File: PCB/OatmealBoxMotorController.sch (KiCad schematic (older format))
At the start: 2 parts

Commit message: Added second motor driver. Got everything hooked up back.
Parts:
- added U7: TB6612FNG, symbol TB6612FNG
- gave numbers to parts that had none: 2
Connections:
- net +12V: now also U7.13 (VM2), U7.14 (VM3), U7.24 (VM1)
- net +3V3: now also U7.19 (STBY), U7.20 (VCC)
- net GND: now also U7.10 (PGND2), U7.18 (GND), U7.3 (PGND1), U7.4 (PGND1), U7.9 (PGND2)
- net at U5.15 (PWM8): now also U7.23 (PWMA)
- net at U5.16 (PWM9): now also U7.22 (AIN2)
- net at U5.17 (PWM10): now also U7.21 (AIN1)
- net at U5.18 (PWM11): now also U7.17 (BIN1)
- net at U5.19 (PWM12): now also U7.16 (BIN2)
- net at U5.20 (PWM13): now also U7.15 (PWMB)
- net ePWM3: now reaches U5.21 (PWM14)
- net ePWM4: now reaches U5.22 (PWM15)
- net ePWM1: now reaches U5.6 (PWM0)
- net ePWM2: now reaches U5.7 (PWM1)
- new net Motor3+: U7.1 (AO1), U7.2 (AO1)
- new net Motor3-: U7.5 (AO2), U7.6 (AO2)
- new net Motor4+: U7.7 (BO2), U7.8 (BO2)
- new net Motor4-: U7.11 (BO1), U7.12 (BO1)
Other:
- moved on the sheet: U5

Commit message: Connected I2C, fixed ERC errors
Connected I2C to the PWM controller.
Fixed ERC errors.
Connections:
- net SCL: now reaches U5.26 (SCL)
- net SDA: now reaches U5.27 (SDA)
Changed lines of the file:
@@
 $EndComp
 $Comp
-L +3.3V #PWR026
+L +3.3V #PWR029
 U 1 1 5B4A7AD7
 P 1000 1450
-F 0 "#PWR026" H 1000 1300 50  0001 C CNN
+F 0 "#PWR029" H 1000 1300 50  0001 C CNN
 F 1 "+3.3V" H 1000 1590 50  0000 C CNN
 F 2 "" H 1000 1450 50  0001 C CNN
@@
 $EndComp
 $Comp
-L GND #PWR027
+L GND #PWR030
 U 1 1 5B4A7AED
 P 950 2250
-F 0 "#PWR027" H 950 2000 50  0001 C CNN
+F 0 "#PWR030" H 950 2000 50  0001 C CNN
 F 1 "GND" H 950 2100 50  0000 C CNN
 F 2 "" H 950 2250 50  0001 C CNN
@@
 $EndComp
 $Comp
-L GND #PWR028
+L GND #PWR031
 U 1 1 5B4A7B03
 P 950 3200
-F 0 "#PWR028" H 950 2950 50  0001 C CNN
+F 0 "#PWR031" H 950 2950 50  0001 C CNN
 F 1 "GND" H 950 3050 50  0000 C CNN
 F 2 "" H 950 3200 50  0001 C CNN
@@
 Connection ~ 1100 2800
 $Comp
-L +3.3V #PWR029
+L +3.3V #PWR032
 U 1 1 5B4A7BB0
 P 950 3000
-F 0 "#PWR029" H 950 2850 50  0001 C CNN
+F 0 "#PWR032" H 950 2850 50  0001 C CNN
 F 1 "+3.3V" H 950 3140 50  0000 C CNN
 F 2 "" H 950 3000 50  0001 C CNN
@@
 $EndComp
 $Comp
-L +12V #PWR030
+L +12V #PWR033
 U 1 1 5B4D75A1
 P 4700 1500
-F 0 "#PWR030" H 4700 1350 50  0001 C CNN
+F 0 "#PWR033" H 4700 1350 50  0001 C CNN
 F 1 "+12V" H 4700 1640 50  0000 C CNN
 F 2 "" H 4700 1500 50  0001 C CNN
@@
 $EndComp
 $Comp
-L +12V #PWR031
+L +12V #PWR034
 U 1 1 5B4D75BD
 P 4700 3300
-F 0 "#PWR031" H 4700 3150 50  0001 C CNN
+F 0 "#PWR034" H 4700 3150 50  0001 C CNN
 F 1 "+12V" H 4700 3440 50  0000 C CNN
 F 2 "" H 4700 3300 50  0001 C CNN
@@
 Connection ~ 4800 3300
 $Comp
-L +3.3V #PWR032
+L +3.3V #PWR035
 U 1 1 5B4D7628
 P 4700 2400
-F 0 "#PWR032" H 4700 2250 50  0001 C CNN
+F 0 "#PWR035" H 4700 2250 50  0001 C CNN
 F 1 "+3.3V" H 4700 2540 50  0000 C CNN
 F 2 "" H 4700 2400 50  0001 C CNN
@@
 Connection ~ 4750 2400
 $Comp
-L GND #PWR033
+L GND #PWR036
 U 1 1 5B4D76CA
 P 4650 2600
-F 0 "#PWR033" H 4650 2350 50  0001 C CNN
+F 0 "#PWR036" H 4650 2350 50  0001 C CNN
 F 1 "GND" H 4650 2450 50  0000 C CNN
 F 2 "" H 4650 2600 50  0001 C CNN
@@
 $EndComp
 $Comp
-L GND #PWR034
+L GND #PWR037
 U 1 1 5B4D76E6
 P 6200 2900
-F 0 "#PWR034" H 6200 2650 50  0001 C CNN
+F 0 "#PWR037" H 6200 2650 50  0001 C CNN
 F 1 "GND" H 6200 2750 50  0000 C CNN
 F 2 "" H 6200 2900 50  0001 C CNN
@@
 $EndComp
 $Comp
-L GND #PWR035
+L GND #PWR038
 U 1 1 5B4D7702
 P 6200 2000
-F 0 "#PWR035" H 6200 1750 50  0001 C CNN
+F 0 "#PWR038" H 6200 1750 50  0001 C CNN
 F 1 "GND" H 6200 1850 50  0000 C CNN
 F 2 "" H 6200 2000 50  0001 C CNN
@@
 $EndComp
 $Comp
-L +12V #PWR036
+L +12V #PWR039
 U 1 1 5B4EDBEA
 P 4750 3700
-F 0 "#PWR036" H 4750 3550 50  0001 C CNN
+F 0 "#PWR039" H 4750 3550 50  0001 C CNN
 F 1 "+12V" H 4750 3840 50  0000 C CNN
 F 2 "" H 4750 3700 50  0001 C CNN
@@
 $EndComp
 $Comp
-L +12V #PWR037
+L +12V #PWR040
 U 1 1 5B4EDBF0
 P 4750 5500
-F 0 "#PWR037" H 4750 5350 50  0001 C CNN
+F 0 "#PWR040" H 4750 5350 50  0001 C CNN
 F 1 "+12V" H 4750 5640 50  0000 C CNN
 F 2 "" H 4750 5500 50  0001 C CNN
@@
 Connection ~ 4850 5500
 $Comp
-L +3.3V #PWR038
+L +3.3V #PWR041
 U 1 1 5B4EDBFC
 P 4750 4600
-F 0 "#PWR038" H 4750 4450 50  0001 C CNN
+F 0 "#PWR041" H 4750 4450 50  0001 C CNN
 F 1 "+3.3V" H 4750 4740 50  0000 C CNN
 F 2 "" H 4750 4600 50  0001 C CNN
@@
 Connection ~ 4800 4600
 $Comp
-L GND #PWR039
+L GND #PWR042
 U 1 1 5B4EDC06
 P 4700 4800
-F 0 "#PWR039" H 4700 4550 50  0001 C CNN
+F 0 "#PWR042" H 4700 4550 50  0001 C CNN
 F 1 "GND" H 4700 4650 50  0000 C CNN
 F 2 "" H 4700 4800 50  0001 C CNN
@@
 $EndComp
 $Comp
-L GND #PWR040
+L GND #PWR043
 U 1 1 5B4EDC0C
 P 6250 5100
-F 0 "#PWR040" H 6250 4850 50  0001 C CNN
+F 0 "#PWR043" H 6250 4850 50  0001 C CNN
 F 1 "GND" H 6250 4950 50  0000 C CNN
 F 2 "" H 6250 5100 50  0001 C CNN
@@
 $EndComp
 $Comp
-L GND #PWR041
+L GND #PWR044
 U 1 1 5B4EDC12
 P 6250 4200
-F 0 "#PWR041" H 6250 3950 50  0001 C CNN
+F 0 "#PWR044" H 6250 3950 50  0001 C CNN
 F 1 "GND" H 6250 4050 50  0000 C CNN
 F 2 "" H 6250 4200 50  0001 C CNN
@@
 Wire Wire Line
 	2550 3200 2400 3200
+Text HLabel 1100 1900 0    60   BiDi ~ 0
+SDA
+Text HLabel 1100 2050 0    60   Input ~ 0
+SCL
+Wire Wire Line
+	1200 1900 1100 1900
+Wire Wire Line
+	1200 2050 1100 2050
 $EndSCHEMATC

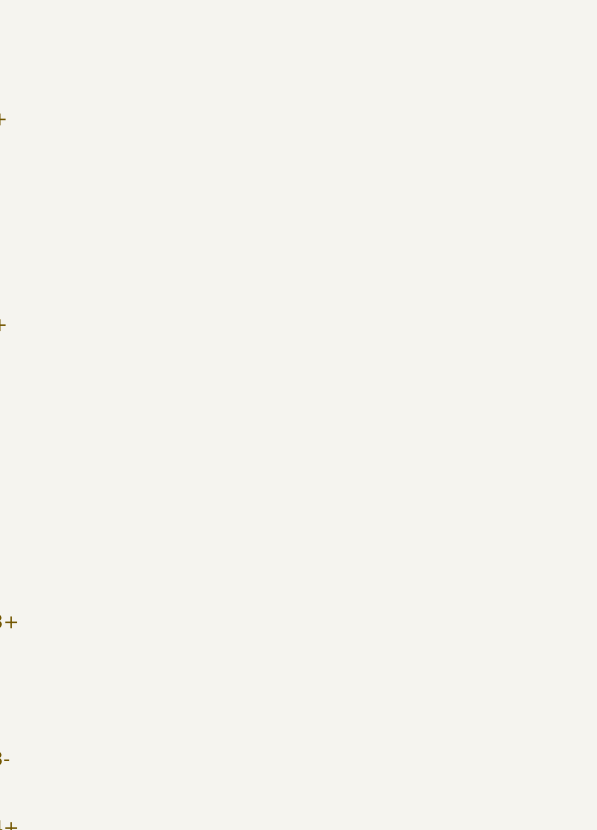
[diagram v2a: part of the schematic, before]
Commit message: Added caps for the motor drivers
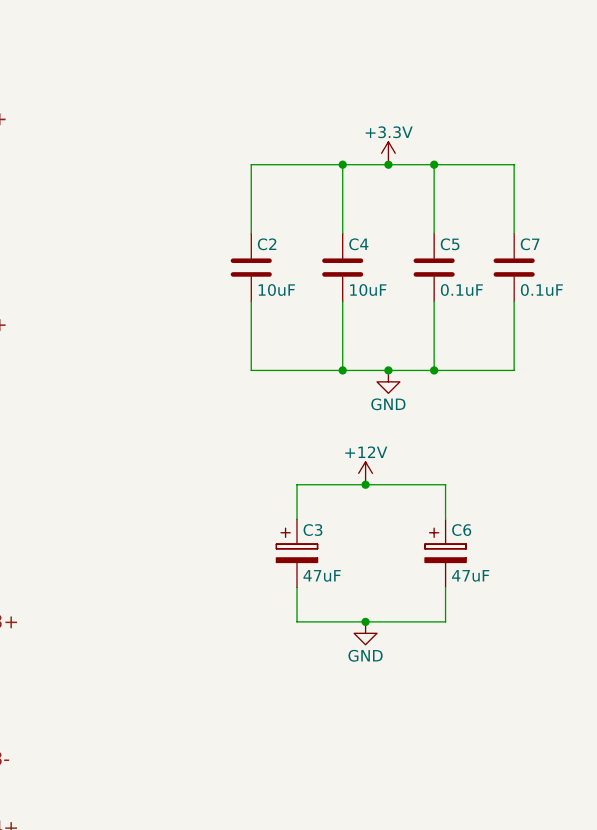
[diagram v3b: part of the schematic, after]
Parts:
- added C2, C4: 10uF, symbol C
- added C3, C6: 47uF, symbol CP
- added C5, C7: 0.1uF, symbol C
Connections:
- net +12V: now also C3.1, C6.1
- net +3V3: now also C2.1, C4.1, C5.1, C7.1
- net GND: now also C2.2, C3.2, C4.2, C5.2, C6.2, C7.2
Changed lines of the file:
@@
 $EndComp
 $Comp
-L +3.3V #PWR029
+L +3.3V #PWR32
 U 1 1 5B4A7AD7
 P 1000 1450
-F 0 "#PWR029" H 1000 1300 50  0001 C CNN
+F 0 "#PWR32" H 1000 1300 50  0001 C CNN
 F 1 "+3.3V" H 1000 1590 50  0000 C CNN
 F 2 "" H 1000 1450 50  0001 C CNN
@@
 $EndComp
 $Comp
-L GND #PWR030
+L GND #PWR29
 U 1 1 5B4A7AED
 P 950 2250
-F 0 "#PWR030" H 950 2000 50  0001 C CNN
+F 0 "#PWR29" H 950 2000 50  0001 C CNN
 F 1 "GND" H 950 2100 50  0000 C CNN
 F 2 "" H 950 2250 50  0001 C CNN
@@
 $EndComp
 $Comp
-L GND #PWR031
+L GND #PWR31
 U 1 1 5B4A7B03
 P 950 3200
-F 0 "#PWR031" H 950 2950 50  0001 C CNN
+F 0 "#PWR31" H 950 2950 50  0001 C CNN
 F 1 "GND" H 950 3050 50  0000 C CNN
 F 2 "" H 950 3200 50  0001 C CNN
@@
 Connection ~ 1100 2800
 $Comp
-L +3.3V #PWR032
+L +3.3V #PWR30
 U 1 1 5B4A7BB0
 P 950 3000
-F 0 "#PWR032" H 950 2850 50  0001 C CNN
+F 0 "#PWR30" H 950 2850 50  0001 C CNN
 F 1 "+3.3V" H 950 3140 50  0000 C CNN
 F 2 "" H 950 3000 50  0001 C CNN
@@
 $EndComp
 $Comp
-L +12V #PWR033
+L +12V #PWR34
 U 1 1 5B4D75A1
 P 4700 1500
-F 0 "#PWR033" H 4700 1350 50  0001 C CNN
+F 0 "#PWR34" H 4700 1350 50  0001 C CNN
 F 1 "+12V" H 4700 1640 50  0000 C CNN
 F 2 "" H 4700 1500 50  0001 C CNN
@@
 $EndComp
 $Comp
-L +12V #PWR034
+L +12V #PWR36
 U 1 1 5B4D75BD
 P 4700 3300
-F 0 "#PWR034" H 4700 3150 50  0001 C CNN
+F 0 "#PWR36" H 4700 3150 50  0001 C CNN
 F 1 "+12V" H 4700 3440 50  0000 C CNN
 F 2 "" H 4700 3300 50  0001 C CNN
@@
 Connection ~ 4800 3300
 $Comp
-L +3.3V #PWR035
+L +3.3V #PWR35
 U 1 1 5B4D7628
 P 4700 2400
-F 0 "#PWR035" H 4700 2250 50  0001 C CNN
+F 0 "#PWR35" H 4700 2250 50  0001 C CNN
 F 1 "+3.3V" H 4700 2540 50  0000 C CNN
 F 2 "" H 4700 2400 50  0001 C CNN
@@
 Connection ~ 4750 2400
 $Comp
-L GND #PWR036
+L GND #PWR33
 U 1 1 5B4D76CA
 P 4650 2600
-F 0 "#PWR036" H 4650 2350 50  0001 C CNN
+F 0 "#PWR33" H 4650 2350 50  0001 C CNN
 F 1 "GND" H 4650 2450 50  0000 C CNN
 F 2 "" H 4650 2600 50  0001 C CNN
@@
 $EndComp
 $Comp
-L GND #PWR037
+L GND #PWR42
 U 1 1 5B4D76E6
 P 6200 2900
-F 0 "#PWR037" H 6200 2650 50  0001 C CNN
+F 0 "#PWR42" H 6200 2650 50  0001 C CNN
 F 1 "GND" H 6200 2750 50  0000 C CNN
 F 2 "" H 6200 2900 50  0001 C CNN
@@
 $EndComp
 $Comp
-L GND #PWR038
+L GND #PWR41
 U 1 1 5B4D7702
 P 6200 2000
-F 0 "#PWR038" H 6200 1750 50  0001 C CNN
+F 0 "#PWR41" H 6200 1750 50  0001 C CNN
 F 1 "GND" H 6200 1850 50  0000 C CNN
 F 2 "" H 6200 2000 50  0001 C CNN
@@
 $EndComp
 $Comp
-L +12V #PWR039
+L +12V #PWR38
 U 1 1 5B4EDBEA
 P 4750 3700
-F 0 "#PWR039" H 4750 3550 50  0001 C CNN
+F 0 "#PWR38" H 4750 3550 50  0001 C CNN
 F 1 "+12V" H 4750 3840 50  0000 C CNN
 F 2 "" H 4750 3700 50  0001 C CNN
@@
 $EndComp
 $Comp
-L +12V #PWR040
+L +12V #PWR40
 U 1 1 5B4EDBF0
 P 4750 5500
-F 0 "#PWR040" H 4750 5350 50  0001 C CNN
+F 0 "#PWR40" H 4750 5350 50  0001 C CNN
 F 1 "+12V" H 4750 5640 50  0000 C CNN
 F 2 "" H 4750 5500 50  0001 C CNN
@@
 Connection ~ 4850 5500
 $Comp
-L +3.3V #PWR041
+L +3.3V #PWR39
 U 1 1 5B4EDBFC
 P 4750 4600
-F 0 "#PWR041" H 4750 4450 50  0001 C CNN
+F 0 "#PWR39" H 4750 4450 50  0001 C CNN
 F 1 "+3.3V" H 4750 4740 50  0000 C CNN
 F 2 "" H 4750 4600 50  0001 C CNN
@@
 Connection ~ 4800 4600
 $Comp
-L GND #PWR042
+L GND #PWR37
 U 1 1 5B4EDC06
 P 4700 4800
-F 0 "#PWR042" H 4700 4550 50  0001 C CNN
+F 0 "#PWR37" H 4700 4550 50  0001 C CNN
 F 1 "GND" H 4700 4650 50  0000 C CNN
 F 2 "" H 4700 4800 50  0001 C CNN
@@
 $EndComp
 $Comp
-L GND #PWR043
+L GND #PWR44
 U 1 1 5B4EDC0C
 P 6250 5100
-F 0 "#PWR043" H 6250 4850 50  0001 C CNN
+F 0 "#PWR44" H 6250 4850 50  0001 C CNN
 F 1 "GND" H 6250 4950 50  0000 C CNN
 F 2 "" H 6250 5100 50  0001 C CNN
@@
 $EndComp
 $Comp
-L GND #PWR044
+L GND #PWR43
 U 1 1 5B4EDC12
 P 6250 4200
-F 0 "#PWR044" H 6250 3950 50  0001 C CNN
+F 0 "#PWR43" H 6250 3950 50  0001 C CNN
 F 1 "GND" H 6250 4050 50  0000 C CNN
 F 2 "" H 6250 4200 50  0001 C CNN
@@
 Wire Wire Line
 	1200 2050 1100 2050
+$Comp
+L C C2
+U 1 1 5B502510
+P 7700 2350
+F 0 "C2" H 7725 2450 50  0000 L CNN
+F 1 "10uF" H 7725 2250 50  0000 L CNN
+F 2 "" H 7738 2200 50  0001 C CNN
+F 3 "" H 7700 2350 50  0001 C CNN
+	1    7700 2350
+	1    0    0    -1
+$EndComp
+$Comp
+L C C4
+U 1 1 5B50255E
+P 8100 2350
+F 0 "C4" H 8125 2450 50  0000 L CNN
+F 1 "10uF" H 8125 2250 50  0000 L CNN
+F 2 "" H 8138 2200 50  0001 C CNN
+F 3 "" H 8100 2350 50  0001 C CNN
+	1    8100 2350
+	1    0    0    -1
+$EndComp
+$Comp
+L C C5
+U 1 1 5B502583
+P 8500 2350
+F 0 "C5" H 8525 2450 50  0000 L CNN
+F 1 "0.1uF" H 8525 2250 50  0000 L CNN
+F 2 "" H 8538 2200 50  0001 C CNN
+F 3 "" H 8500 2350 50  0001 C CNN
+	1    8500 2350
+	1    0    0    -1
+$EndComp
+$Comp
+L C C7
+U 1 1 5B5025A6
+P 8850 2350
+F 0 "C7" H 8875 2450 50  0000 L CNN
+F 1 "0.1uF" H 8875 2250 50  0000 L CNN
+F 2 "" H 8888 2200 50  0001 C CNN
+F 3 "" H 8850 2350 50  0001 C CNN
+	1    8850 2350
+	1    0    0    -1
+$EndComp
+$Comp
+L GND #PWR48
+U 1 1 5B5025CB
+P 8300 2800
+F 0 "#PWR48" H 8300 2550 50  0001 C CNN
+F 1 "GND" H 8300 2650 50  0000 C CNN
+F 2 "" H 8300 2800 50  0001 C CNN
+F 3 "" H 8300 2800 50  0001 C CNN
+	1    8300 2800
+	1    0    0    -1
+$EndComp
+$Comp
+L +3.3V #PWR47
+U 1 1 5B5025ED
+P 8300 1900
+F 0 "#PWR47" H 8300 1750 50  0001 C CNN
+F 1 "+3.3V" H 8300 2040 50  0000 C CNN
+F 2 "" H 8300 1900 50  0001 C CNN
+F 3 "" H 8300 1900 50  0001 C CNN
+	1    8300 1900
+	1    0    0    -1
+$EndComp
+Wire Wire Line
+	7700 2800 8850 2800
+Wire Wire Line
+	8850 2800 8850 2500
+Wire Wire Line
+	8500 2500 8500 2800
+Connection ~ 8500 2800
+Wire Wire Line
+	7700 2800 7700 2500
+Connection ~ 8300 2800
+Wire Wire Line
+	8100 2500 8100 2800
+Connection ~ 8100 2800
+Wire Wire Line
+	7700 2200 7700 1900
+Wire Wire Line
+	7700 1900 8850 1900
+Wire Wire Line
+	8100 2200 8100 1900
+Connection ~ 8100 1900
+Wire Wire Line
+	8850 1900 8850 2200
+Connection ~ 8300 1900
+Wire Wire Line
+	8500 2200 8500 1900
+Connection ~ 8500 1900
+$Comp
+L CP C3
+U 1 1 5B502D2A
+P 7900 3600
+F 0 "C3" H 7925 3700 50  0000 L CNN
+F 1 "47uF" H 7925 3500 50  0000 L CNN
+F 2 "" H 7938 3450 50  0001 C CNN
+F 3 "" H 7900 3600 50  0001 C CNN
+	1    7900 3600
+	1    0    0    -1
+$EndComp
+$Comp
+L CP C6
+U 1 1 5B502D5A
+P 8550 3600
+F 0 "C6" H 8575 3700 50  0000 L CNN
+F 1 "47uF" H 8575 3500 50  0000 L CNN
+F 2 "" H 8588 3450 50  0001 C CNN
+F 3 "" H 8550 3600 50  0001 C CNN
+	1    8550 3600
+	1    0    0    -1
+$EndComp
+$Comp
+L GND #PWR46
+U 1 1 5B502E04
+P 8200 3900
+F 0 "#PWR46" H 8200 3650 50  0001 C CNN
+F 1 "GND" H 8200 3750 50  0000 C CNN
+F 2 "" H 8200 3900 50  0001 C CNN
+F 3 "" H 8200 3900 50  0001 C CNN
+	1    8200 3900
+	1    0    0    -1
+$EndComp
+$Comp
+L +12V #PWR45
+U 1 1 5B502E3C
+P 8200 3300
+F 0 "#PWR45" H 8200 3150 50  0001 C CNN
+F 1 "+12V" H 8200 3440 50  0000 C CNN
+F 2 "" H 8200 3300 50  0001 C CNN
+F 3 "" H 8200 3300 50  0001 C CNN
+	1    8200 3300
+	1    0    0    -1
+$EndComp
+Wire Wire Line
+	7900 3450 7900 3300
+Wire Wire Line
+	7900 3300 8550 3300
+Wire Wire Line
+	8550 3300 8550 3450
+Connection ~ 8200 3300
+Wire Wire Line
+	8550 3900 8550 3750
+Wire Wire Line
+	7900 3900 8550 3900
+Wire Wire Line
+	7900 3750 7900 3900
+Connection ~ 8200 3900
 $EndSCHEMATC

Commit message: Cleaned up, renamed a few things and added all footprints.
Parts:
- C2, C3, C4, C6: footprint (none) -> Capacitors_ThroughHole:CP_Radial_D5.0mm_P2.50mm
- C5, C7: footprint (none) -> Capacitors_SMD:C_0805_HandSoldering
- U5: footprint (none) -> Housings_SSOP:TSSOP-28_4.4x9.7mm_Pitch0.65mm
- U6, U7: footprint (none) -> Housings_SSOP:SSOP-24_5.3x8.2mm_Pitch0.65mm
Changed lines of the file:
@@
 F 0 "U5" H 1800 1600 60  0000 C CNN
 F 1 "PCA9685" H 1800 3300 60  0000 C CNN
-F 2 "" H 1900 2450 60  0001 C CNN
+F 2 "Housings_SSOP:TSSOP-28_4.4x9.7mm_Pitch0.65mm" H 1900 2450 60  0001 C CNN
 F 3 "" H 1900 2450 60  0001 C CNN
 	1    1800 2450
@@
 $EndComp
 $Comp
-L +3.3V #PWR32
+L +3.3V #PWR029
 U 1 1 5B4A7AD7
 P 1000 1450
-F 0 "#PWR32" H 1000 1300 50  0001 C CNN
+F 0 "#PWR029" H 1000 1300 50  0001 C CNN
 F 1 "+3.3V" H 1000 1590 50  0000 C CNN
 F 2 "" H 1000 1450 50  0001 C CNN
@@
 $EndComp
 $Comp
-L GND #PWR29
+L GND #PWR030
 U 1 1 5B4A7AED
 P 950 2250
-F 0 "#PWR29" H 950 2000 50  0001 C CNN
+F 0 "#PWR030" H 950 2000 50  0001 C CNN
 F 1 "GND" H 950 2100 50  0000 C CNN
 F 2 "" H 950 2250 50  0001 C CNN
@@
 $EndComp
 $Comp
-L GND #PWR31
+L GND #PWR031
 U 1 1 5B4A7B03
 P 950 3200
-F 0 "#PWR31" H 950 2950 50  0001 C CNN
+F 0 "#PWR031" H 950 2950 50  0001 C CNN
 F 1 "GND" H 950 3050 50  0000 C CNN
 F 2 "" H 950 3200 50  0001 C CNN
@@
 Connection ~ 1100 2800
 $Comp
-L +3.3V #PWR30
+L +3.3V #PWR032
 U 1 1 5B4A7BB0
 P 950 3000
-F 0 "#PWR30" H 950 2850 50  0001 C CNN
+F 0 "#PWR032" H 950 2850 50  0001 C CNN
 F 1 "+3.3V" H 950 3140 50  0000 C CNN
 F 2 "" H 950 3000 50  0001 C CNN
@@
 F 0 "U6" H 5400 1600 60  0000 C CNN
 F 1 "TB6612FNG" H 5400 3400 60  0000 C CNN
-F 2 "" H 5400 2500 60  0001 C CNN
+F 2 "Housings_SSOP:SSOP-24_5.3x8.2mm_Pitch0.65mm" H 5400 2500 60  0001 C CNN
 F 3 "" H 5400 2500 60  0001 C CNN
 	1    5400 2500
@@
 $EndComp
 $Comp
-L +12V #PWR34
+L +12V #PWR033
 U 1 1 5B4D75A1
 P 4700 1500
-F 0 "#PWR34" H 4700 1350 50  0001 C CNN
+F 0 "#PWR033" H 4700 1350 50  0001 C CNN
 F 1 "+12V" H 4700 1640 50  0000 C CNN
 F 2 "" H 4700 1500 50  0001 C CNN
@@
 $EndComp
 $Comp
-L +12V #PWR36
+L +12V #PWR034
 U 1 1 5B4D75BD
 P 4700 3300
-F 0 "#PWR36" H 4700 3150 50  0001 C CNN
+F 0 "#PWR034" H 4700 3150 50  0001 C CNN
 F 1 "+12V" H 4700 3440 50  0000 C CNN
 F 2 "" H 4700 3300 50  0001 C CNN
@@
 Connection ~ 4800 3300
 $Comp
-L +3.3V #PWR35
+L +3.3V #PWR035
 U 1 1 5B4D7628
 P 4700 2400
-F 0 "#PWR35" H 4700 2250 50  0001 C CNN
+F 0 "#PWR035" H 4700 2250 50  0001 C CNN
 F 1 "+3.3V" H 4700 2540 50  0000 C CNN
 F 2 "" H 4700 2400 50  0001 C CNN
@@
 Connection ~ 4750 2400
 $Comp
-L GND #PWR33
+L GND #PWR036
 U 1 1 5B4D76CA
 P 4650 2600
-F 0 "#PWR33" H 4650 2350 50  0001 C CNN
+F 0 "#PWR036" H 4650 2350 50  0001 C CNN
 F 1 "GND" H 4650 2450 50  0000 C CNN
 F 2 "" H 4650 2600 50  0001 C CNN
@@
 $EndComp
 $Comp
-L GND #PWR42
+L GND #PWR037
 U 1 1 5B4D76E6
 P 6200 2900
-F 0 "#PWR42" H 6200 2650 50  0001 C CNN
+F 0 "#PWR037" H 6200 2650 50  0001 C CNN
 F 1 "GND" H 6200 2750 50  0000 C CNN
 F 2 "" H 6200 2900 50  0001 C CNN
@@
 $EndComp
 $Comp
-L GND #PWR41
+L GND #PWR038
 U 1 1 5B4D7702
 P 6200 2000
-F 0 "#PWR41" H 6200 1750 50  0001 C CNN
+F 0 "#PWR038" H 6200 1750 50  0001 C CNN
 F 1 "GND" H 6200 1850 50  0000 C CNN
 F 2 "" H 6200 2000 50  0001 C CNN
@@
 F 0 "U7" H 5450 3800 60  0000 C CNN
 F 1 "TB6612FNG" H 5450 5600 60  0000 C CNN
-F 2 "" H 5450 4700 60  0001 C CNN
+F 2 "Housings_SSOP:SSOP-24_5.3x8.2mm_Pitch0.65mm" H 5450 4700 60  0001 C CNN
 F 3 "" H 5450 4700 60  0001 C CNN
 	1    5450 4700
@@
 $EndComp
 $Comp
-L +12V #PWR38
+L +12V #PWR039
 U 1 1 5B4EDBEA
 P 4750 3700
-F 0 "#PWR38" H 4750 3550 50  0001 C CNN
+F 0 "#PWR039" H 4750 3550 50  0001 C CNN
 F 1 "+12V" H 4750 3840 50  0000 C CNN
 F 2 "" H 4750 3700 50  0001 C CNN
@@
 $EndComp
 $Comp
-L +12V #PWR40
+L +12V #PWR040
 U 1 1 5B4EDBF0
 P 4750 5500
-F 0 "#PWR40" H 4750 5350 50  0001 C CNN
+F 0 "#PWR040" H 4750 5350 50  0001 C CNN
 F 1 "+12V" H 4750 5640 50  0000 C CNN
 F 2 "" H 4750 5500 50  0001 C CNN
@@
 Connection ~ 4850 5500
 $Comp
-L +3.3V #PWR39
+L +3.3V #PWR041
 U 1 1 5B4EDBFC
 P 4750 4600
-F 0 "#PWR39" H 4750 4450 50  0001 C CNN
+F 0 "#PWR041" H 4750 4450 50  0001 C CNN
 F 1 "+3.3V" H 4750 4740 50  0000 C CNN
 F 2 "" H 4750 4600 50  0001 C CNN
@@
 Connection ~ 4800 4600
 $Comp
-L GND #PWR37
+L GND #PWR042
 U 1 1 5B4EDC06
 P 4700 4800
-F 0 "#PWR37" H 4700 4550 50  0001 C CNN
+F 0 "#PWR042" H 4700 4550 50  0001 C CNN
 F 1 "GND" H 4700 4650 50  0000 C CNN
 F 2 "" H 4700 4800 50  0001 C CNN
@@
 $EndComp
 $Comp
-L GND #PWR44
+L GND #PWR043
 U 1 1 5B4EDC0C
 P 6250 5100
-F 0 "#PWR44" H 6250 4850 50  0001 C CNN
+F 0 "#PWR043" H 6250 4850 50  0001 C CNN
 F 1 "GND" H 6250 4950 50  0000 C CNN
 F 2 "" H 6250 5100 50  0001 C CNN
@@
 $EndComp
 $Comp
-L GND #PWR43
+L GND #PWR044
 U 1 1 5B4EDC12
 P 6250 4200
-F 0 "#PWR43" H 6250 3950 50  0001 C CNN
+F 0 "#PWR044" H 6250 3950 50  0001 C CNN
 F 1 "GND" H 6250 4050 50  0000 C CNN
 F 2 "" H 6250 4200 50  0001 C CNN
@@
 F 0 "C2" H 7725 2450 50  0000 L CNN
 F 1 "10uF" H 7725 2250 50  0000 L CNN
-F 2 "" H 7738 2200 50  0001 C CNN
+F 2 "Capacitors_ThroughHole:CP_Radial_D5.0mm_P2.50mm" H 7738 2200 50  0001 C CNN
 F 3 "" H 7700 2350 50  0001 C CNN
 	1    7700 2350
@@
 F 0 "C4" H 8125 2450 50  0000 L CNN
 F 1 "10uF" H 8125 2250 50  0000 L CNN
-F 2 "" H 8138 2200 50  0001 C CNN
+F 2 "Capacitors_ThroughHole:CP_Radial_D5.0mm_P2.50mm" H 8138 2200 50  0001 C CNN
 F 3 "" H 8100 2350 50  0001 C CNN
 	1    8100 2350
@@
 F 0 "C5" H 8525 2450 50  0000 L CNN
 F 1 "0.1uF" H 8525 2250 50  0000 L CNN
-F 2 "" H 8538 2200 50  0001 C CNN
+F 2 "Capacitors_SMD:C_0805_HandSoldering" H 8538 2200 50  0001 C CNN
 F 3 "" H 8500 2350 50  0001 C CNN
 	1    8500 2350
@@
 F 0 "C7" H 8875 2450 50  0000 L CNN
 F 1 "0.1uF" H 8875 2250 50  0000 L CNN
-F 2 "" H 8888 2200 50  0001 C CNN
+F 2 "Capacitors_SMD:C_0805_HandSoldering" H 8888 2200 50  0001 C CNN
 F 3 "" H 8850 2350 50  0001 C CNN
 	1    8850 2350
@@
 $EndComp
 $Comp
-L GND #PWR48
+L GND #PWR045
 U 1 1 5B5025CB
 P 8300 2800
-F 0 "#PWR48" H 8300 2550 50  0001 C CNN
+F 0 "#PWR045" H 8300 2550 50  0001 C CNN
 F 1 "GND" H 8300 2650 50  0000 C CNN
 F 2 "" H 8300 2800 50  0001 C CNN
@@
 $EndComp
 $Comp
-L +3.3V #PWR47
+L +3.3V #PWR046
 U 1 1 5B5025ED
 P 8300 1900
-F 0 "#PWR47" H 8300 1750 50  0001 C CNN
+F 0 "#PWR046" H 8300 1750 50  0001 C CNN
 F 1 "+3.3V" H 8300 2040 50  0000 C CNN
 F 2 "" H 8300 1900 50  0001 C CNN
@@
 F 0 "C3" H 7925 3700 50  0000 L CNN
 F 1 "47uF" H 7925 3500 50  0000 L CNN
-F 2 "" H 7938 3450 50  0001 C CNN
+F 2 "Capacitors_ThroughHole:CP_Radial_D5.0mm_P2.50mm" H 7938 3450 50  0001 C CNN
 F 3 "" H 7900 3600 50  0001 C CNN
 	1    7900 3600
@@
 F 0 "C6" H 8575 3700 50  0000 L CNN
 F 1 "47uF" H 8575 3500 50  0000 L CNN
-F 2 "" H 8588 3450 50  0001 C CNN
+F 2 "Capacitors_ThroughHole:CP_Radial_D5.0mm_P2.50mm" H 8588 3450 50  0001 C CNN
 F 3 "" H 8550 3600 50  0001 C CNN
 	1    8550 3600
@@
 $EndComp
 $Comp
-L GND #PWR46
+L GND #PWR047
 U 1 1 5B502E04
 P 8200 3900
-F 0 "#PWR46" H 8200 3650 50  0001 C CNN
+F 0 "#PWR047" H 8200 3650 50  0001 C CNN
 F 1 "GND" H 8200 3750 50  0000 C CNN
 F 2 "" H 8200 3900 50  0001 C CNN
@@
 $EndComp
 $Comp
-L +12V #PWR45
+L +12V #PWR048
 U 1 1 5B502E3C
 P 8200 3300
-F 0 "#PWR45" H 8200 3150 50  0001 C CNN
+F 0 "#PWR048" H 8200 3150 50  0001 C CNN
 F 1 "+12V" H 8200 3440 50  0000 C CNN
 F 2 "" H 8200 3300 50  0001 C CNN
